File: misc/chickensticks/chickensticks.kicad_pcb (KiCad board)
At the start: 4 copper layers, 42 x 100 mm, 102 parts, among them J1 Conn_01x05_Pin, J10 Conn_01x03_Pin, J2 HRO_TYPE-C-31-M-12, J3 Conn_01x04, J4 Conn_01x06, J5 Conn_01x06, J6 Conn_01x04, J7 Conn_01x04, J8 S02-25200300, J9 SMA, Q1 Si2371EDS, Q2 DMG9926UDM, Q3 2N7002, SW1 SKRPANE010, SW2 EC11E18244AU, U1 USBLC6-2SC6, U2 STM32L433CCTx, U3 TJA1042T-3, U4 LR2021IMLTRT, U5 LP5907MFX-3.3, U6 MCP73831-2-MC, U7 BQ29700, Y1 25 MHz, Y2 TG2520SMN 32.0000M-MCGNNM0

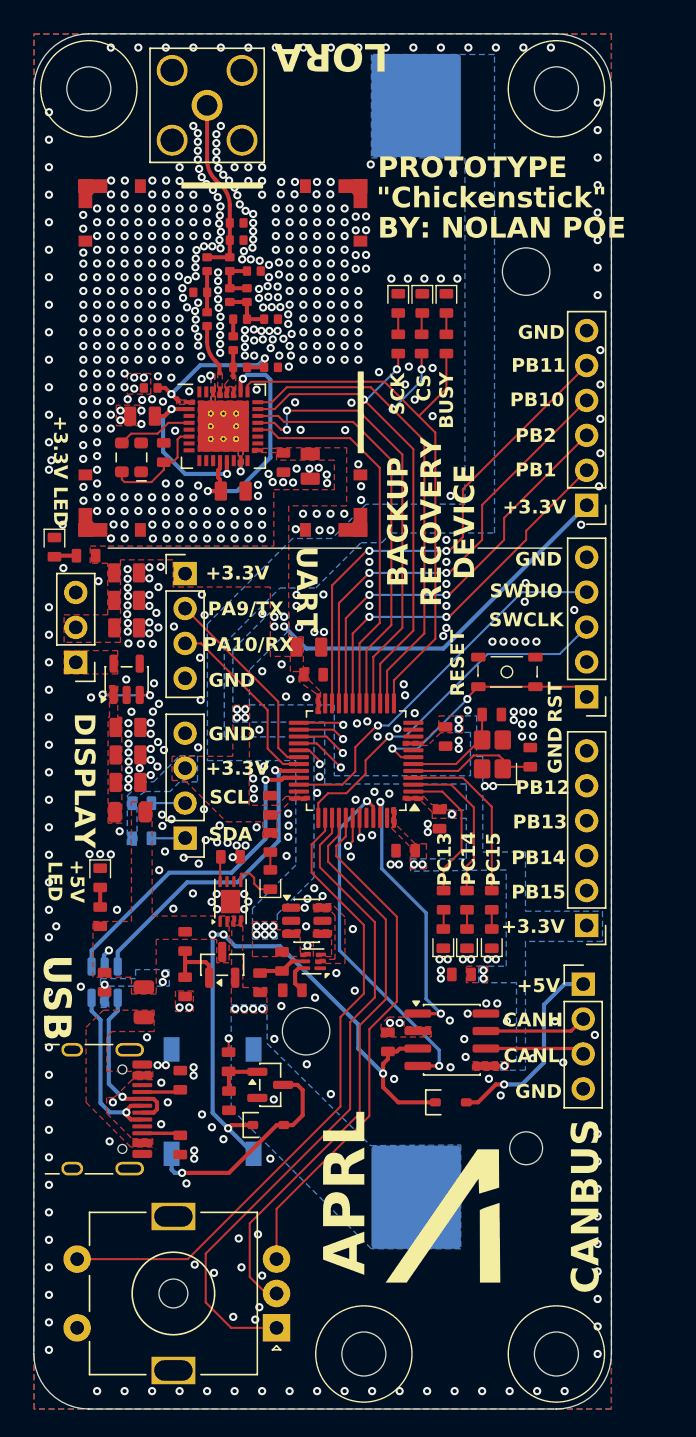
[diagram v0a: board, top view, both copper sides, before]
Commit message: Simplify chickensticks, get isospi-tx ready, and update some cubemx projects
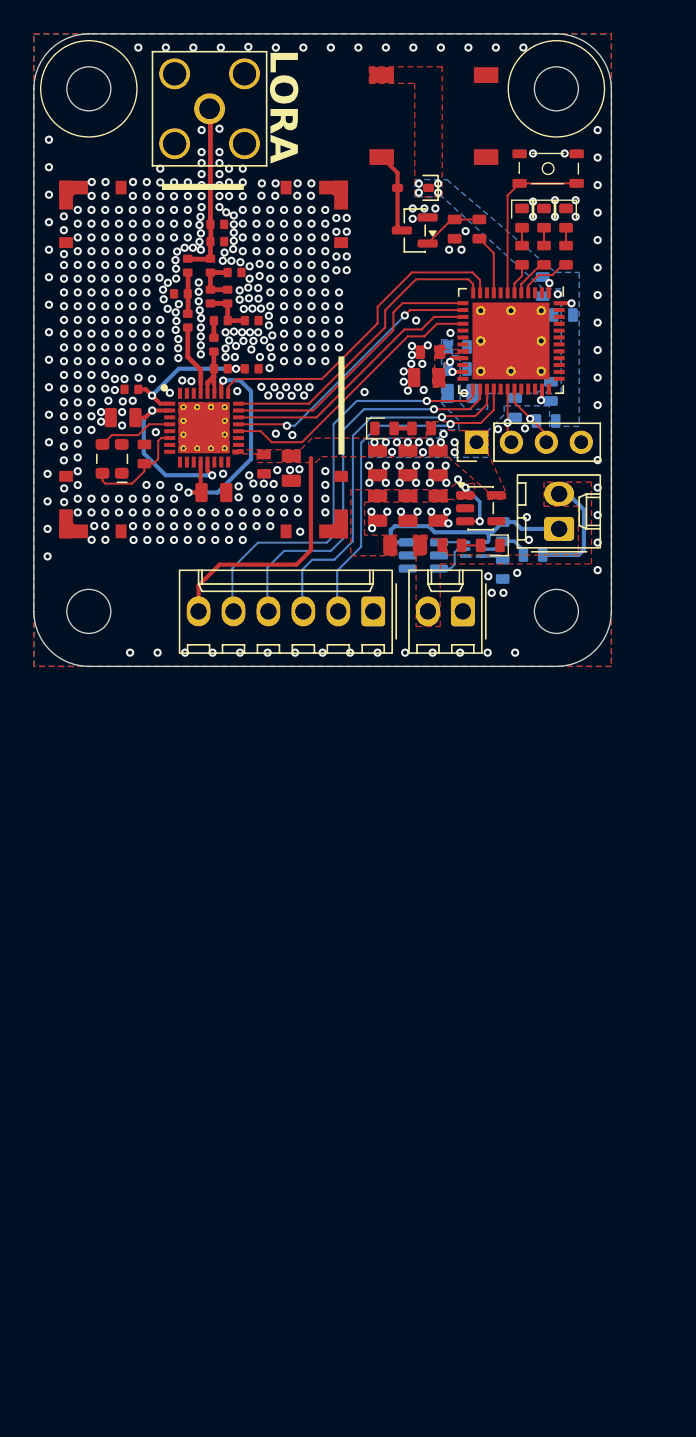
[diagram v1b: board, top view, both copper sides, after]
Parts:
- removed BT1: 18650, Battery:BatteryHolder_Keystone_1042_1x18650
- removed C10, C11: 100n, APRL_Passive:C_0603
- removed C9: 10pF, APRL_Passive:C_0603
- removed D1: MM3Z10VT1G, APRL_Passive:SOD-323
- removed D11, D6, D7, D8: LED_Small, APRL_Passive:LED_0603
- removed F1: 500mA, APRL_Passive:Fuse_0805_2012Metric
- removed J10: Conn_01x03_Pin, Connector_PinHeader_2.54mm:PinHeader_1x03_P2.54mm_Vertical
- removed J4, J5: Conn_01x06, Connector_PinHeader_2.54mm:PinHeader_1x06_P2.54mm_Vertical
- removed J6: Conn_01x04, Connector_PinHeader_2.54mm:PinHeader_1x04_P2.54mm_Vertical
- removed Q1: Si2371EDS, Package_TO_SOT_SMD:SOT-23
- removed R1, R2: 5.1k, APRL_Passive:R_0603
- removed R10, R15, R8, R9: 10k, APRL_Passive:R_0603
- removed R13: 100R, APRL_Passive:R_0603
- removed R14: 100k, APRL_Passive:R_0603
- removed R17: 2k, APRL_Passive:R_0603
- removed REF**: APRL_Logo_2Layer-v1, APRL_Graphic:APRL_Logo_2Layer-v1
- removed SW2: EC11E18244AU, APRL_Module:RotaryEncoder_Alps_EC11E-Switch_Vertical_H20mm_MountingHoles
- removed U1: USBLC6-2SC6, Package_TO_SOT_SMD:SOT-23-6
- removed U2: STM32L433CCTx, Package_QFP:LQFP-48_7x7mm_P0.5mm
- removed U3: TJA1042T-3, Package_SO:SOIC-8_3.9x4.9mm_P1.27mm
- removed U6: MCP73831-2-MC, APRL_Package:DFN-8-1EP_3x2mm_P0.5mm_EP1.7x1.4mm
- removed Y1: 25 MHz, APRL_Passive:3225-4P-L
- added U8: STM32G431CBU6, APRL_Package_QFN:QFN-48_EP_7.3x7.3_Pitch0.5mm, F.Cu at (144.1, 86.6)
- BZ1: moved to F.Cu
- C1, C2, C3, C32, C4, C5, C6, Q2, R16, R18, U7: moved to B.Cu
- C7: value 100n -> 100nF
- C8: value 10pF -> 1uF; footprint APRL_Passive:C_0603 -> APRL_Passive:C_0805
- J1: value Conn_01x05_Pin -> Conn_01x02; footprint Connector_PinHeader_2.54mm:PinHeader_1x05_P2.54mm_Vertical -> Connector_Molex:Molex_KK-254_AE-6410-02A_1x02_P2.54mm_Vertical
- J2: value HRO_TYPE-C-31-M-12 -> Conn_01x02; footprint APRL_Connector:USB_C_Receptacle_HRO_TYPE-C-31-M-12 -> Connector_Molex:Molex_KK-254_AE-6410-02A_1x02_P2.54mm_Vertical
- J3: value Conn_01x04 -> Conn_01x06; footprint Connector_PinHeader_2.54mm:PinHeader_1x04_P2.54mm_Vertical -> Connector_Molex:Molex_KK-254_AE-6410-06A_1x06_P2.54mm_Vertical
- U5: value LP5907MFX-3.3 -> AP2112K-3.3
- moved BZ1 79.0 mm to (134.7, 67.3), turned to 0 degrees
- moved D5 69.0 mm to (137.0, 75.5), turned to 180 degrees
- moved R19 65.5 mm to (140.0, 78.5)
- moved R20 63.2 mm to (141.8, 78.5), turned to 90 degrees
- moved Q3 63.0 mm to (137.1, 78.6), turned to 180 degrees
- moved H3 57.6 mm to (113.4, 106.3)
- moved J2 54.4 mm to (147.6, 100.3), turned to 90 degrees
- moved H4 54.0 mm to (147.4, 106.3)
- moved D2 52.9 mm to (146.5, 77.7), turned to -90 degrees
- moved D4 52.7 mm to (148.1, 77.7), turned to -90 degrees
- moved D3 52.5 mm to (144.9, 77.7), turned to -90 degrees
- moved C7 51.6 mm to (138.2, 87.5), turned to 180 degrees
- moved R3 47.5 mm to (146.5, 80.4), turned to 90 degrees
- moved R5 47.2 mm to (148.1, 80.4), turned to 90 degrees
- moved R4 47.1 mm to (144.9, 80.4), turned to 90 degrees
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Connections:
- net /LoRa Transceiver/LORA_OUT renamed Net-(J9-In)
- net /LoRa Transceiver/LORA_RFI_LF renamed Net-(U4-RFI_LF)
- net /LoRa Transceiver/LORA_RFI_RF1 renamed Net-(C23-Pad2)
- net /LoRa Transceiver/LORA_RFO_LF_1 renamed Net-(U4-RFO_LF1)
- net /LoRa Transceiver/LORA_RFO_LF_2 renamed Net-(C17-Pad1)
- net /LoRa Transceiver/LORA_RFO_LF_3 renamed Net-(C16-Pad1)
- net /LoRa Transceiver/LORA_RFO_LF_4 renamed Net-(C16-Pad2)
- net /LoRa Transceiver/LORA_VR_PA renamed Net-(U4-VR_PA)
- net /Microcontroller/DISP_SCL renamed Net-(J7-Pin_2)
- BZ1 pad 1: +VUSB -> +3.3V
- BZ1 pad 3: +VBAT -> unconnected-(BZ1-Pad3)
- BZ1 pad 4: GND -> unconnected-(BZ1-Pad4)
- C32 pad 2: Net-(BT1--) -> Net-(J2-Pin_1)
- C7 pad 1: GND -> Net-(U8-VREF+)
- C7 pad 2: +VUSB -> GND
- C8 pad 1: Net-(U2-PH0) -> Net-(U8-VREF+)
- D5 pad 1: +VUSB -> +3.3V
- F2 pad 1: +VUSB -> +VIN
- J1 pad 1: /Microcontroller/~{RST} -> GND
- J1 pad 2: +3.3V_EXT -> +VIN
- J3 pad 1: +3.3V -> GND
- J3 pad 2: /Microcontroller/UART_TX -> Net-(J3-Pin_2)
- J3 pad 3: /Microcontroller/UART_RX -> Net-(J3-Pin_3)
- J3 pad 4: GND -> Net-(J3-Pin_4)
- J7 pad 1: /Microcontroller/DISP_SDA -> +3.3V
- J7 pad 3: +3.3V -> Net-(J7-Pin_3)
- Q2 pad 3: Net-(BT1--) -> Net-(J2-Pin_1)
- R11 pad 1: +VUSB -> +VIN
- R16 pad 1: +VBAT -> +VIN
- R20 pad 1: /Microcontroller/BUZZER -> Net-(U8-PA1)
- R6 pad 2: /Microcontroller/DISP_SDA -> Net-(J7-Pin_3)
- U5 pad 5: /Power/3.3_LDO_OUT -> +3.3V
- U7 pad 4: Net-(BT1--) -> Net-(J2-Pin_1)
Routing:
- net /Microcontroller/ENC_A: track 48.3 -> 0.00 mm
- net /Microcontroller/ENC_SW: track 47.4 -> 0.00 mm
- net +VUSB: track 47.2 -> 0.00 mm, vias 5 -> 0
- net /Microcontroller/ENC_C: track 41.3 -> 0.00 mm
- net /Microcontroller/ENC_B: track 37.8 -> 0.00 mm
- net /Microcontroller/PB11: track 35.8 -> 0.00 mm, vias 2 -> 0
- net /Microcontroller/BUZZER: track 34.1 -> 0.00 mm, vias 2 -> 0
- net /Microcontroller/PB10: track 32.9 -> 0.00 mm, vias 2 -> 0
- net Net-(J3-Pin_5): track 0.00 -> 31.0 mm, vias 0 -> 1
- net /Microcontroller/PB2: track 30.1 -> 0.00 mm, vias 2 -> 0
- net Net-(J3-Pin_4): track 0.00 -> 29.0 mm, vias 0 -> 1
- net /Microcontroller/SWDIO: track 27.8 -> 0.00 mm, vias 1 -> 0
- net /Microcontroller/PB1: track 27.4 -> 0.00 mm, vias 2 -> 0
- net Net-(J3-Pin_3): track 0.00 -> 27.0 mm, vias 0 -> 1
- net /Microcontroller/SWCLK: track 26.5 -> 0.00 mm, vias 1 -> 0
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- added copper zone on F.Cu, net +VIN
- added copper zone on F.Cu, net Net-(U8-VREF+)
- removed copper zone on F.Cu, net (none)
- removed copper zone on In2.Cu, net +3.3V_EXT
- removed copper zone on B.Cu, net +VBAT
- removed copper zone on F.Cu, net +VBAT
- removed copper zone on F.Cu, net +VUSB
- removed copper zone on F.Cu, net /Power/3.3_LDO_OUT
- removed copper zone on B.Cu, net Net-(BT1--)
- removed copper zone on F.Cu, net Net-(BT1--)
- removed copper zone on F.Cu, net Net-(F1-Pad1)
- removed copper zone on F.Cu, net Net-(Q2-G1)
- removed copper zone on F.Cu, net Net-(Q2-G2)
- removed copper zone on F.Cu, net Net-(U4-RFI_LF)
- removed copper zone on F.Cu, net Net-(U4-RFO_LF1)
- removed copper zone on F.Cu, net Net-(U4-VR_PA)
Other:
- board size 42 x 100 mm -> 42 x 46 mm
- board text removed: "+3.3V"
- board text removed: "+3.3V LED"
- board text removed: "+5V"
- board text removed: "+5V LED"
- board text removed: "BACKUP RECOVERY DEVICE"
- board text removed: "BUSY"
- board text removed: "BY: NOLAN POE"
- board text removed: "CANBUS"
- board text removed: "CANH"
- board text removed: "CANL"
- board text removed: "CS"
- board text removed: "DISPLAY"
- board text removed: "GND"
- board text removed: "HA↗HA↘HA↗HA↘HA↗HA↘HA↗"
- board text removed: "PA10/RX"
- board text removed: "PA9/TX"
- board text removed: "PB1"
- board text removed: "PB10"
- board text removed: "PB11"
- board text removed: "PB12"
- board text removed: "PB13"
- board text removed: "PB14"
- board text removed: "PB15"
- board text removed: "PB2"
- board text removed: "PC13"
- board text removed: "PC14"
- board text removed: "PC15"
- board text removed: "PROTOTYPE"
- board text removed: "RESET"
- board text removed: "RST"
- board text removed: "SCK"
- board text removed: "SCL"
- board text removed: "SDA"
- board text removed: "SWCLK"
- board text removed: "SWDIO"
- board text removed: "UART"
- board text removed: "USB"
- board text removed: "{dblquote}Chickenstick{dblquote}"
- board text removed: "​ APRL ​"

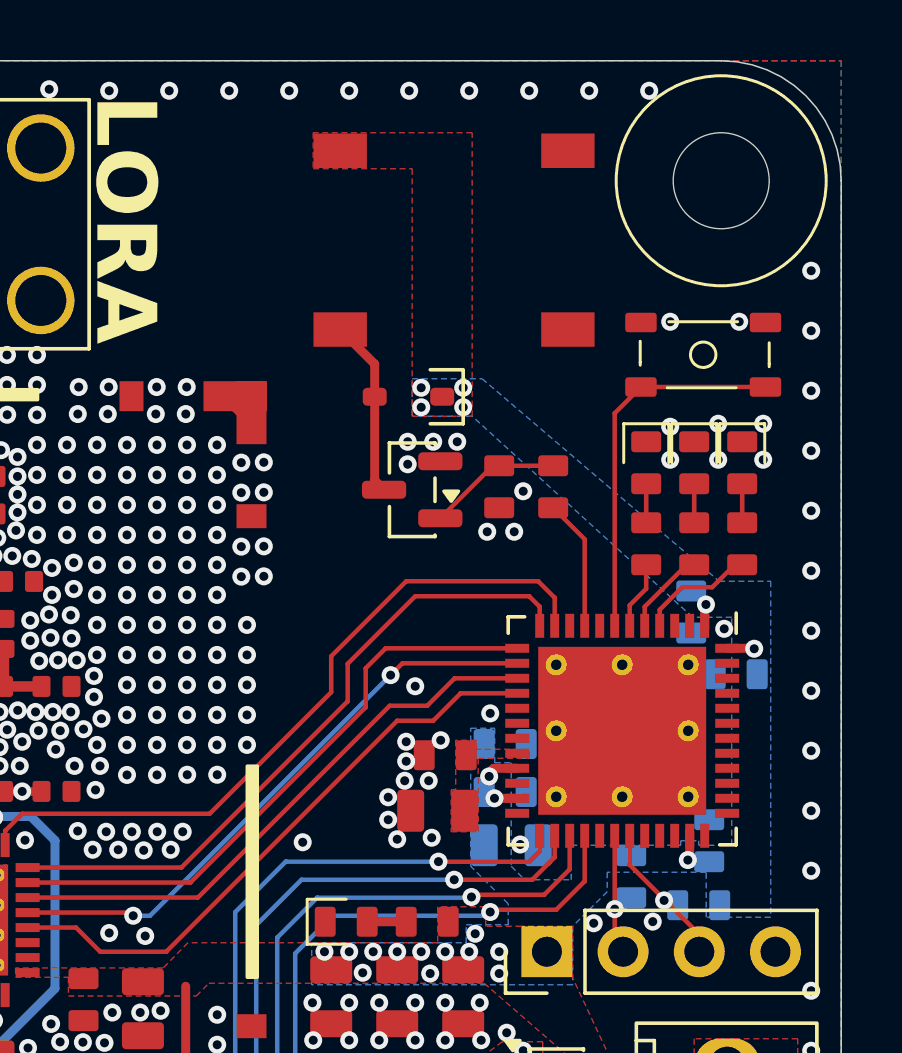
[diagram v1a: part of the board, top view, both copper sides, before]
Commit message: Remove gps, add debug connector to chickensticks, and update rules for isospi and cs
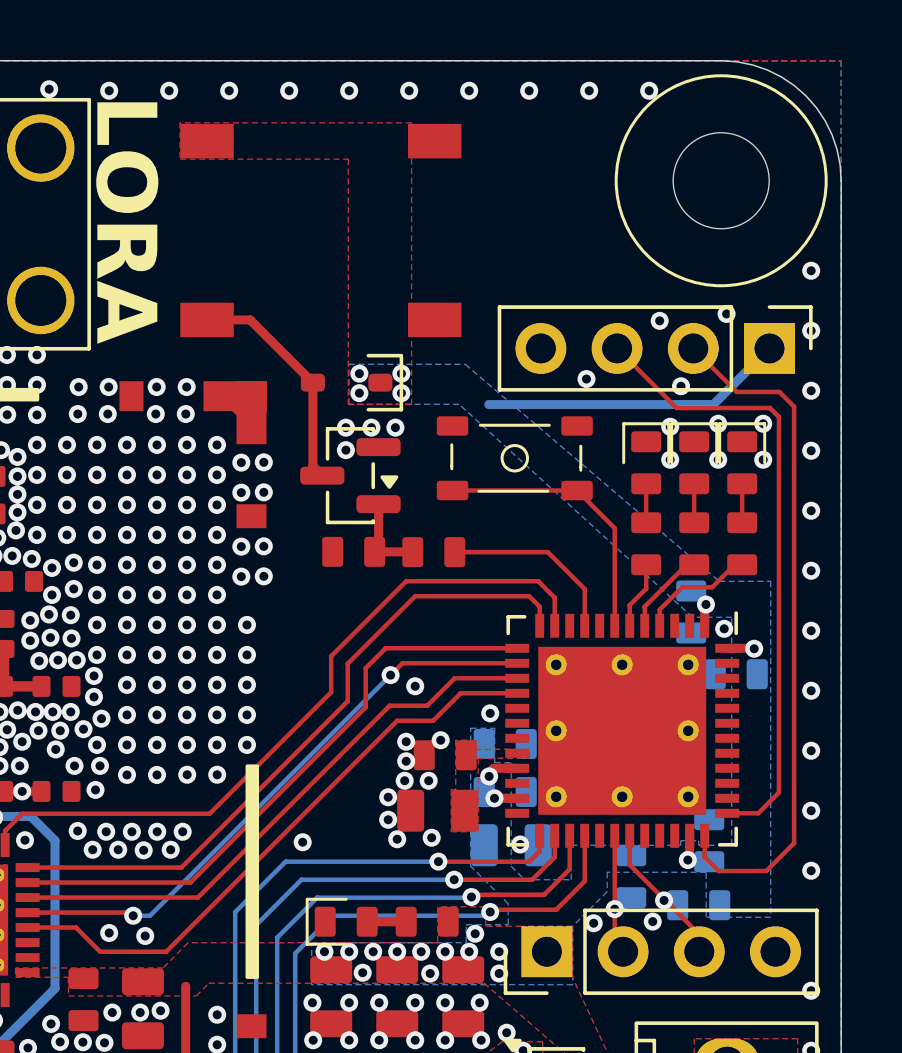
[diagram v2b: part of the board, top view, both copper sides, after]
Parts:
- added J10: Conn_01x04, Connector_PinHeader_2.54mm:PinHeader_1x04_P2.54mm_Vertical, F.Cu at (149.0, 73.9)
- moved SW1 7.17 mm to (140.5, 77.5)
- moved R19 5.31 mm to (135.2, 80.7), turned to 180 degrees
- moved R20 4.54 mm to (137.8, 80.7), turned to 180 degrees
- moved BZ1 4.45 mm to (130.3, 67.0)
- moved D5 2.11 mm to (134.9, 75.0)
- moved Q3 2.11 mm to (135.0, 78.1)
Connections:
- U8 pad 36: /Microcontroller/SWDIO -> Net-(J10-Pin_2)
- U8 pad 37: /Microcontroller/SWCLK -> Net-(J10-Pin_3)
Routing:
- net Net-(J10-Pin_2): track 0.00 -> 23.0 mm
- net Net-(J10-Pin_3): track 0.00 -> 20.9 mm
- net +3.3V: track 22.5 -> 32.7 mm
- net /Microcontroller/~{RST}: track 12.6 -> 9.18 mm
- net Net-(BZ1--): track 5.95 -> 7.63 mm
- net Net-(Q3-G): track 4.49 -> 2.92 mm
- net Net-(U8-PA1): track 4.49 -> 6.06 mm
- net GND: vias 538 -> 537
